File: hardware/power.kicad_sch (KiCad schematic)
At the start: 38 parts, among them U1 INA186A3, U2 TPS61022, U24 SGM40661, U3 TPS2116, U4 LP5912-3.3, U5 TPS22810

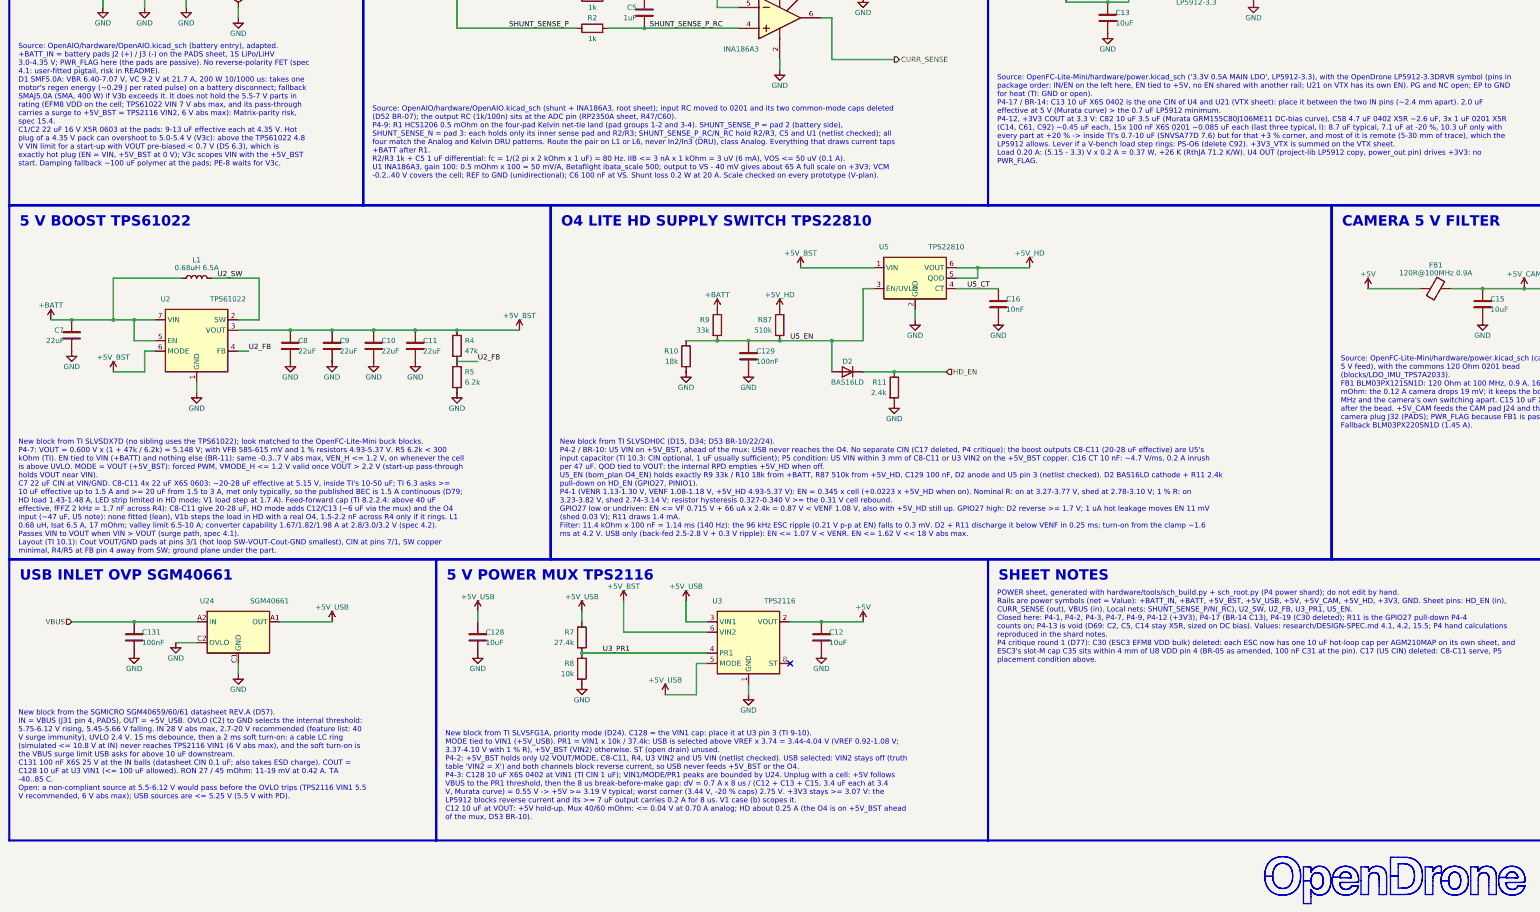
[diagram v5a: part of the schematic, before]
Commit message: schematic: review complete (4 rounds; U20 pin 1 to GND, footprint filters fixed, TPS22810DRVR, R54 270R); ERC 0 errors, check_netlist 7/7; D85-D87
Co-Authored-By: Claude Opus 5.5 <noreply@anthropic.com>
Claude-Session: https://claude.ai/code/session_01RFaS5jnC9tnPam9GBgmGnG
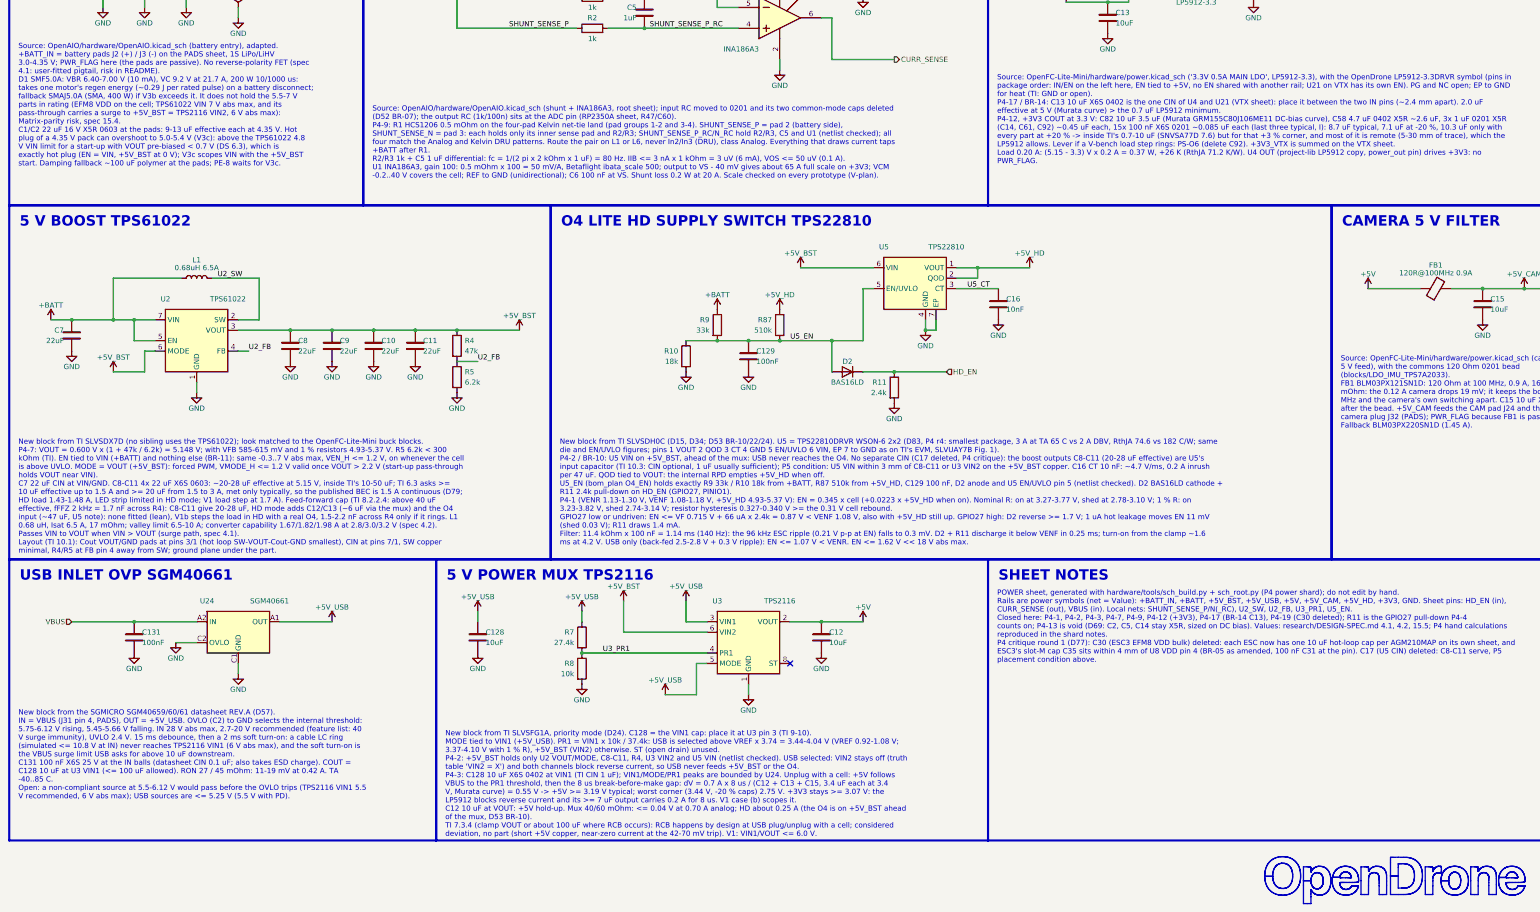
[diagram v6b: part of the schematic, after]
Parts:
- D2: symbol Device:D -> lib:D_BAS16LD
- L1: symbol Device:L -> lib:L_FTC252012
- R1: symbol Device:R_Shunt -> lib:R_Shunt_Kelvin
- U5: footprint lib:SOT-23-6_L2.9-W1.6-P0.95-LS2.8-BR_Dense -> lib:WSON-6-1EP_2x2mm_P0.65mm_EP1x1.6mm_Dense; symbol lib:TPS22810DBVR -> lib:TPS22810DRVR; LCSC C205990 -> (none); MPN TPS22810DBVR -> TPS22810DRVR
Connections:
- net +5V_BST: now also U5.6 (VIN); no longer U5.1 (VIN)
- net +5V_HD: now also U5.1 (VOUT), U5.2 (QOD); no longer U5.5 (QOD), U5.6 (VOUT)
- net GND: now also U5.4 (GND), U5.7 (EP); no longer U5.2 (GND)
- net U5_CT: now also U5.3 (CT); no longer U5.4 (CT)
- net U5_EN: now also U5.5 (EN/UVLO); no longer U5.3 (EN/UVLO)
